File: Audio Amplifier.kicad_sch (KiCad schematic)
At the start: 32 parts, among them J1 AudioJack3, SW1 SW_SPST, U1 TPA3110D2PWP

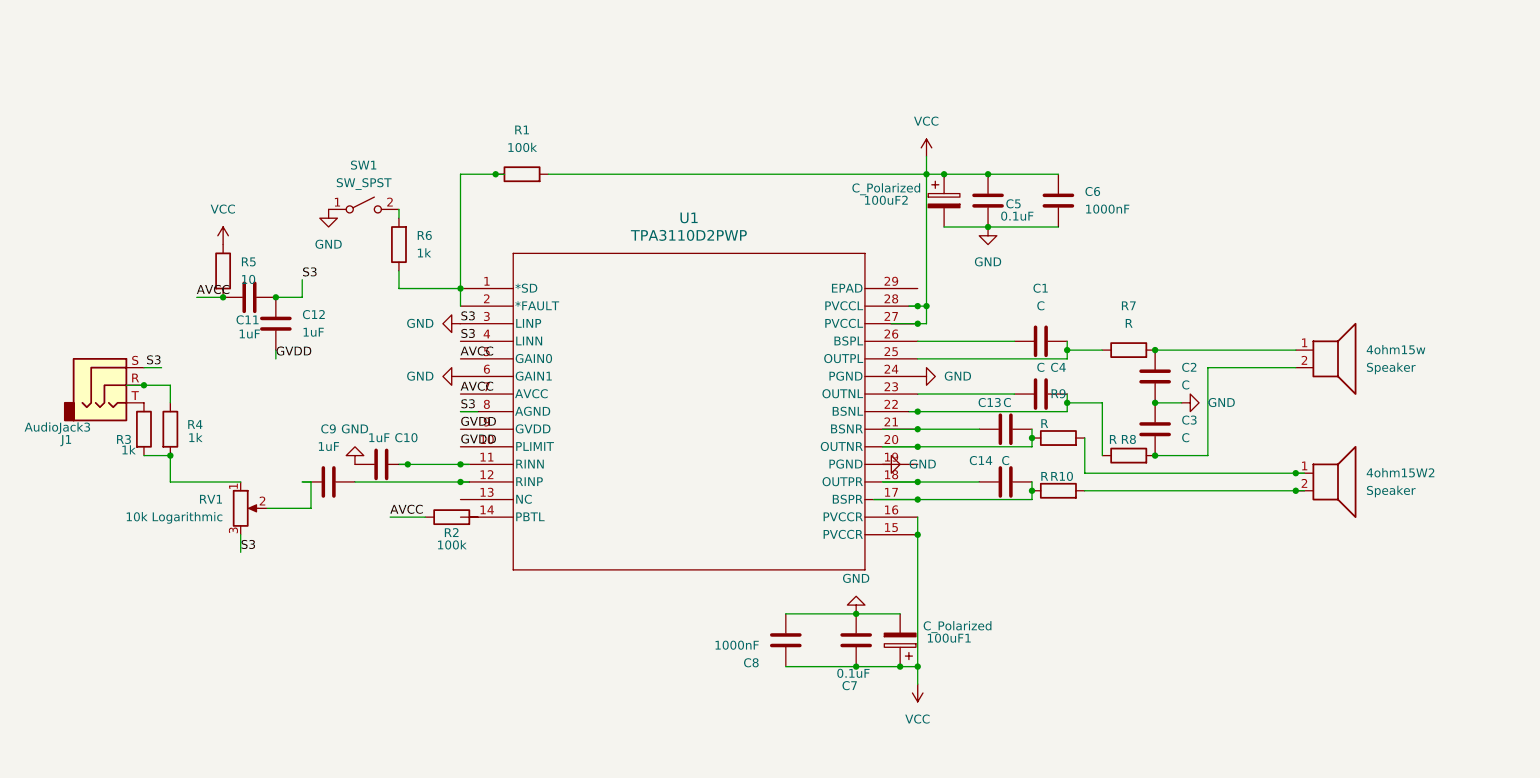
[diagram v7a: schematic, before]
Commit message: Fix(Input): Swapped from the mono input configuration to the stereo BTL config. Switched to dual-gang potentiometer.
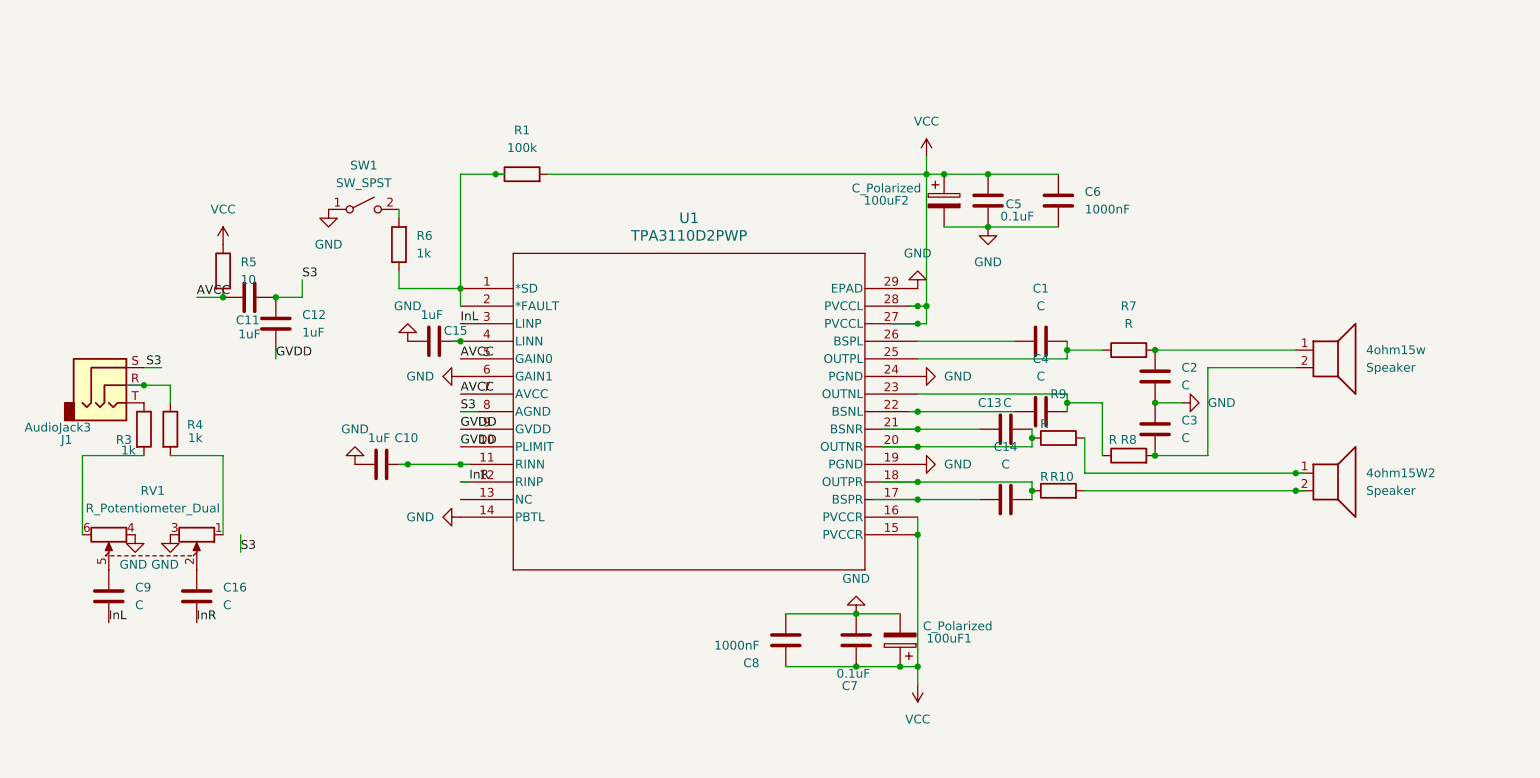
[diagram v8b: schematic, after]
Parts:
- removed R2: 100k, symbol Device:R
- removed RV1: 10k Logarithmic, symbol Device:R_Potentiometer
- added C15: 1uF, symbol Device:C
- added C16: C, symbol Device:C
- added RV1: R_Potentiometer_Dual, symbol Device:R_Potentiometer_Dual
- C9: value 1uF -> C
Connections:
- net GND: now also U1.14 (PBTL), U1.19 (PGND), U1.29 (EPAD), C15.1, RV1.3, RV1.4; no longer C11.2, C12.1, J1.S, U1.3 (LINP), U1.4 (LINN), U1.8 (AGND)
- net InL: now reaches C9.2
- net InL: now also U1.3 (LINP); no longer U1.12 (RINP)
- net at C14.2, R10.1: now also U1.18 (OUTPR); no longer U1.17 (BSPR)
- net at C14.1: now also U1.17 (BSPR); no longer U1.18 (OUTPR)
- net at C4.2, R8.1: now also U1.23 (OUTNL); no longer U1.22 (BSNL)
- net at C4.1: now also U1.22 (BSNL); no longer U1.23 (OUTNL)
- net at C9.1: now also RV1.5
- net at R4.2: now also RV1.1; no longer R3.2
- new net: C15.2, U1.4 (LINN)
- new net: C16.1, RV1.2
- new net: R3.2, RV1.6
- new net InR: C16.2, U1.12 (RINP)
- new net S3: C11.2, C12.1, J1.S, U1.8 (AGND)
